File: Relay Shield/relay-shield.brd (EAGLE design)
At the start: 59.7 x 35.6 mm, 7 parts

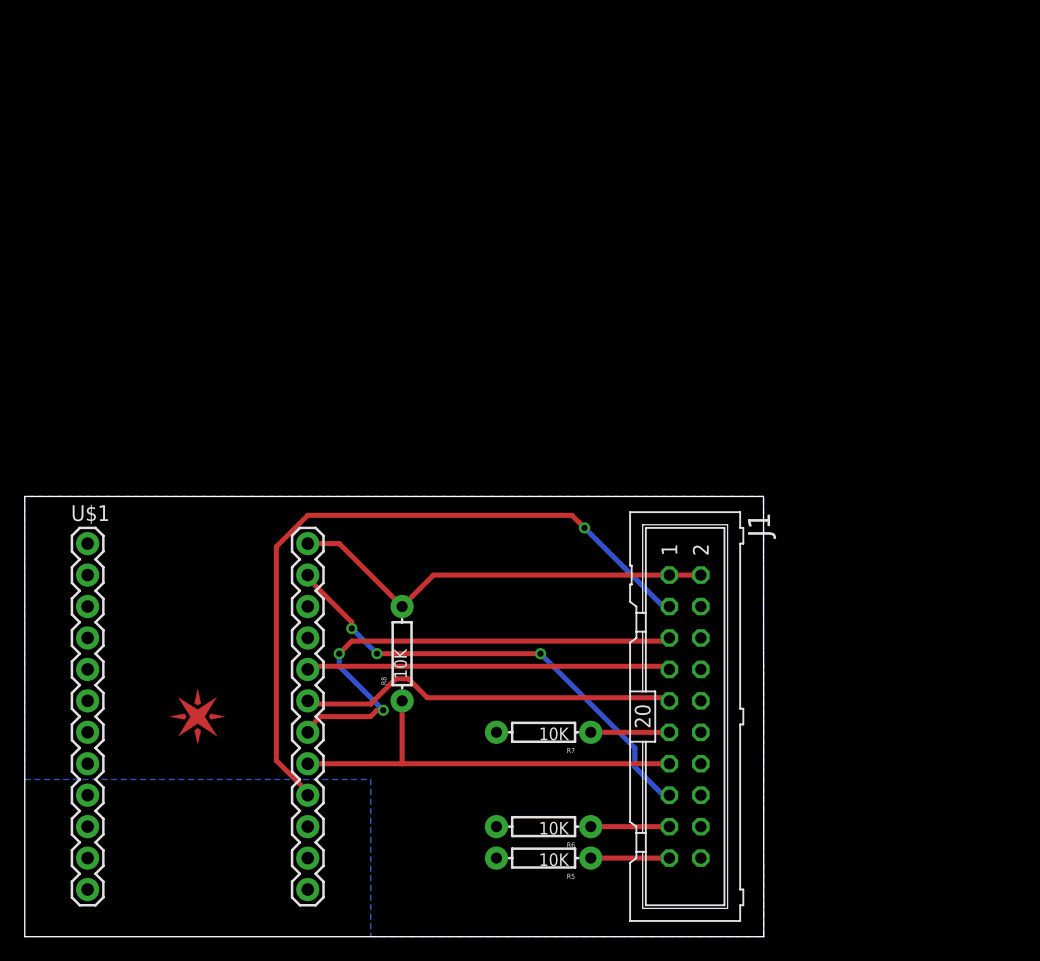
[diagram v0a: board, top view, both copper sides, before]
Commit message: WIP: Moved relay shield from programmer shield folder (last commit was bad)
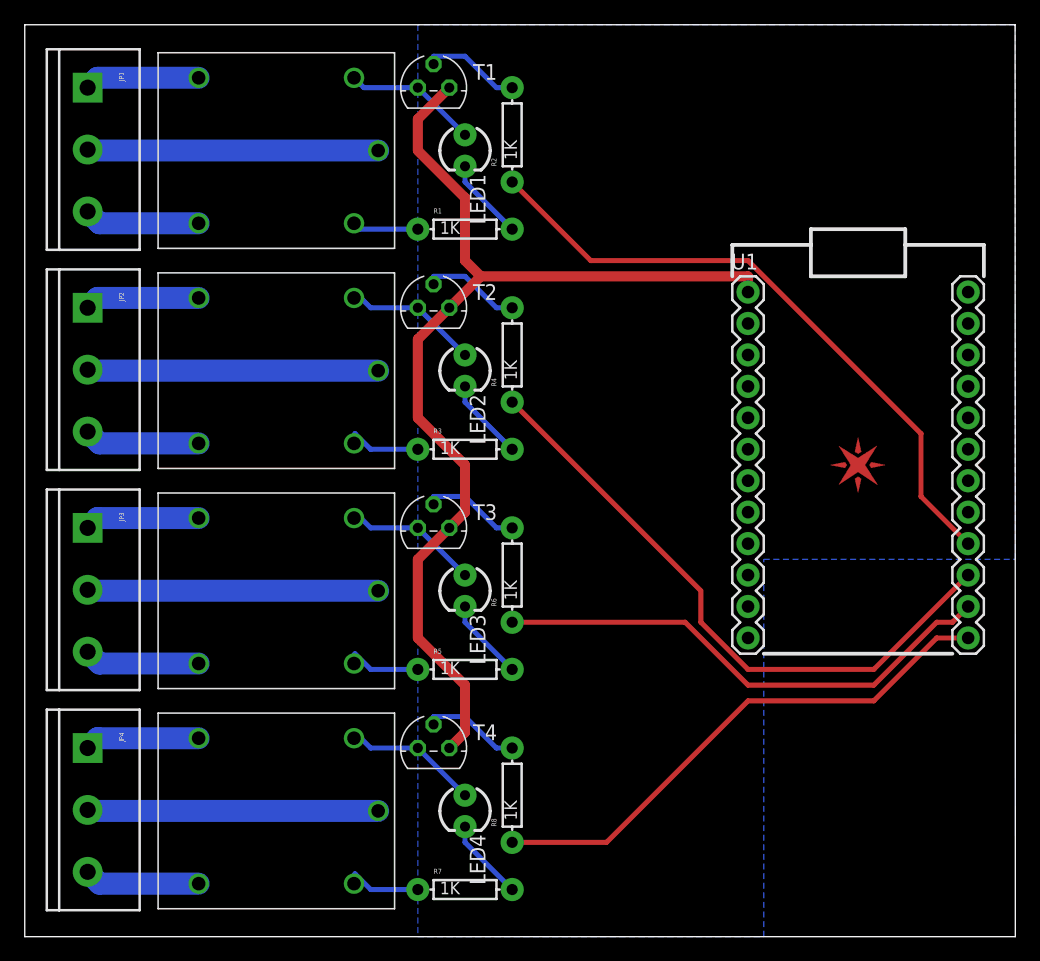
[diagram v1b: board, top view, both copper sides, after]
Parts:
- removed J1: (no value), con-harting-ml:ML20
- removed U$1: SPARK_CORECORE, Spark:SPARK_CORE
- added JP1, JP2, JP3, JP4: (no value), SparkFun-Connectors:SCREWTERMINAL-5MM-3
- added LED1, LED2, LED3, LED4: (no value), SparkFun-LED:LED3MM
- added R1, R2, R3, R4: 1K, SparkFun-Passives:AXIAL-0.3
- added T1, T2, T3, T4: 2N3904, transistor:TO92
- added U1: SPARK_CORECORE, Spark:SPARK_CORE
- added U2, U3, U4, U5: RELAYSONGLE, Spark:SRD-5VDC-SL-C
- R5, R6, R7, R8: value 10K -> 1K
- moved E$1 57.1 mm to (67.3, 38.1)
- moved R6 20.5 mm to (39.4, 29.2), turned to 90 degrees
- moved R5 16.5 mm to (35.6, 21.6), turned to 0 degrees
- moved R8 14.5 mm to (39.4, 11.4)
- moved R7 14.2 mm to (35.6, 3.81), turned to 0 degrees
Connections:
- removed net !RST: J1.15, U$1.23
- removed net +3V3: J1.1, J1.2, R8.P$2, U$1.24
- removed net N$13: J1.19, R5.P$1
- removed net N$14: J1.17, R6.P$1
- removed net N$15: J1.11, R7.P$1
- removed net RAW: U$1.1
- removed net TCK: J1.9, U$1.19
- removed net TDI: J1.5, U$1.18
- removed net TDO: J1.13, R8.P$1, U$1.17
- removed net TMS: J1.7, U$1.20
- removed net TRST: J1.3, U$1.16
- new net +5V: T1.1, T2.1, T3.1, T4.1, U1.1
- new net MAIN1: JP1.2, U2.COMMON
- new net MAIN2: JP2.2, U3.COMMON
- new net MAIN3: JP3.2, U4.COMMON
- new net MAIN4: JP4.2, U5.COMMON
- new net N$1: LED1.A, T1.3, U2.COIL1
- new net N$10: LED4.A, T4.3, U5.COIL1
- new net N$11: R8.P$2, T4.2
- new net N$12: LED4.K, R7.P$2
- new net N$2: LED2.A, T2.3, U3.COIL1
- new net N$3: R2.P$2, T1.2
- new net N$4: LED1.K, R1.P$2
- new net N$5: R4.P$2, T2.2
- new net N$6: LED2.K, R3.P$2
- new net N$7: LED3.A, T3.3, U4.COIL1
- new net N$8: R6.P$2, T3.2
- new net N$9: LED3.K, R5.P$2
- new net NC1: JP1.3, U2.CLOSED
- new net NC2: JP2.3, U3.CLOSED
- new net NC3: JP3.3, U4.CLOSED
- new net NC4: JP4.3, U5.CLOSED
- new net NO1: JP1.1, U2.OPEN
- new net NO2: JP2.1, U3.OPEN
- new net NO3: JP3.1, U4.OPEN
- new net NO4: JP4.1, U5.OPEN
- new net RELAY1: R2.P$1, U1.16
- new net RELAY2: R4.P$1, U1.15
- new net RELAY3: R6.P$1, U1.14
- new net RELAY4: R8.P$1, U1.13
- new net VCC: U1.24
- net GND: now also R1.P$1, R3.P$1, R5.P$1, R7.P$1, U1.2, U1.21, U2.COIL2, U3.COIL2, U4.COIL2, U5.COIL2; no longer J1.10, J1.12, J1.14, J1.16, J1.18, J1.20, J1.4, J1.6, J1.8, R5.P$2, R6.P$2, R7.P$2, U$1.2, U$1.21
- net VDDA: now also U1.22; no longer U$1.22
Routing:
- net +5V: track 0.00 -> 86.7 mm
- net TRST: track 57.2 -> 0.00 mm, vias 1 -> 0
- net RELAY1: track 0.00 -> 51.9 mm
- net RELAY2: track 0.00 -> 50.4 mm
- net RELAY4: track 0.00 -> 43.7 mm
- net RELAY3: track 0.00 -> 41.6 mm
- net TDI: track 40.2 -> 0.00 mm, vias 2 -> 0
- net !RST: track 38.1 -> 0.00 mm, vias 3 -> 0
- net +3V3: track 34.9 -> 0.00 mm
- net TDO: track 34.3 -> 0.00 mm
- net TCK: track 31.0 -> 0.00 mm
- net TMS: track 29.6 -> 0.00 mm
- net GND: track 0.00 -> 24.6 mm
- net MAIN4: track 0.00 -> 23.5 mm
- net MAIN3: track 0.00 -> 23.5 mm
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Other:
- board size 59.7 x 35.6 mm -> 80 x 73.7 mm
- board text added: "2013-04-15"
- board text added: "Spark Relay Shield"
- board text removed: "2013-04-02"
- board text removed: "Spark Programmer Shield"
